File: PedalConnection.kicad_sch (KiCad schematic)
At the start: 17 parts, among them U1 OPA325IDBVR, U10 OPA325IDBVR, U3 VOM618A-3T

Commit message: made connector match drawing
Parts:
- renumbered C6 to C3, C3 to C4, R8 to R15, R11 to R16, R22 to R17, R1 to R18, R23 to R19, R2 to R20, R24 to R21, R3 to R22, R25 to R23, R4 to R24, R26 to R25, R5 to R26, U3 to U7, U10 to U8, U1 to U9
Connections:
- net GNDp is gone; now on net GND: U7.2

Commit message: placed most components
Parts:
- R18: renamed from R15; footprint (none) -> Resistor_SMD:R_0805_2012Metric
- R19: renamed from R16; footprint (none) -> Resistor_SMD:R_0805_2012Metric
- R20: renamed from R17; footprint (none) -> Resistor_SMD:R_0805_2012Metric
- R21: renamed from R18; footprint (none) -> Resistor_SMD:R_0805_2012Metric
- R22: renamed from R19; footprint (none) -> Resistor_SMD:R_0805_2012Metric
- R23: renamed from R20; footprint (none) -> Resistor_SMD:R_0805_2012Metric
- R24: renamed from R21; footprint (none) -> Resistor_SMD:R_0805_2012Metric
- R25: renamed from R22; footprint (none) -> Resistor_SMD:R_0805_2012Metric
- R26: renamed from R23; footprint (none) -> Resistor_SMD:R_0805_2012Metric
- R27: renamed from R24; footprint (none) -> Resistor_SMD:R_0805_2012Metric
- R28: renamed from R25; footprint (none) -> Resistor_SMD:R_0805_2012Metric
- R29: renamed from R26; footprint (none) -> Resistor_SMD:R_0805_2012Metric
- renumbered C3 to C6, C4 to C7, U8 to U10, U9 to U11, U7 to U9

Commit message: Finalized analog components. Everything is done 🙏
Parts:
- removed R28, R29: R_US, Resistor_SMD:R_0805_2012Metric, symbol Device:R_US
- added R6: 100R, Resistor_SMD:R_0805_2012Metric, symbol Device:R_US
- added R7: 10k, Resistor_SMD:R_0805_2012Metric, symbol Device:R_US
- C6, C7: footprint (none) -> Capacitor_SMD:C_0805_2012Metric
- R20: value R_US -> 100R
- R21, R22, R23, R24, R26: value R_US -> 10k
- R25, R27: value R_US -> 1k
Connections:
- net BrakeIO: now also R27.2
- net GND: now also R21.1, R23.1, R6.2; no longer R21.2, R25.1, R27.1
- net Throttle+: now also R6.1, R7.1; no longer R21.1, R23.1
- net ThrottleIO: now also R25.2
- net at U11.1 (OUT): now also R23.2, R25.1; no longer R27.2
- net at R26.2, U10.1 (OUT): now also R27.1
- new net: R21.2, R7.2, U11.3 (+IN)

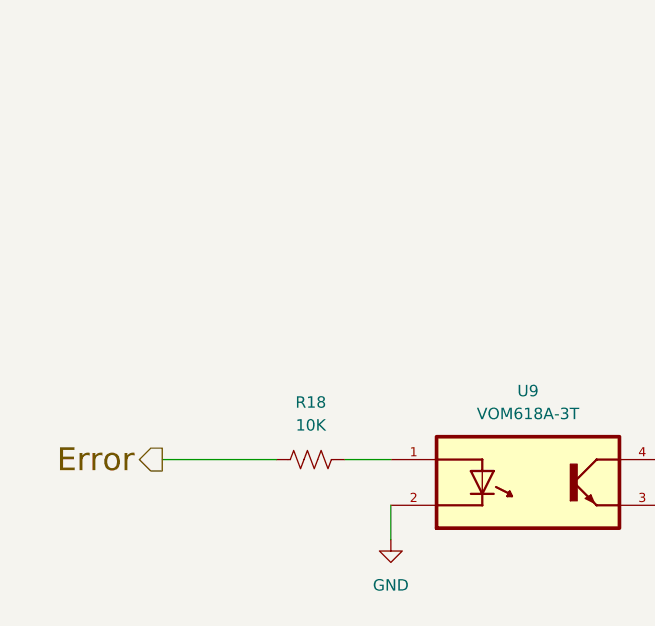
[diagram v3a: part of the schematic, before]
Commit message: added LED indicators, fixed footprints
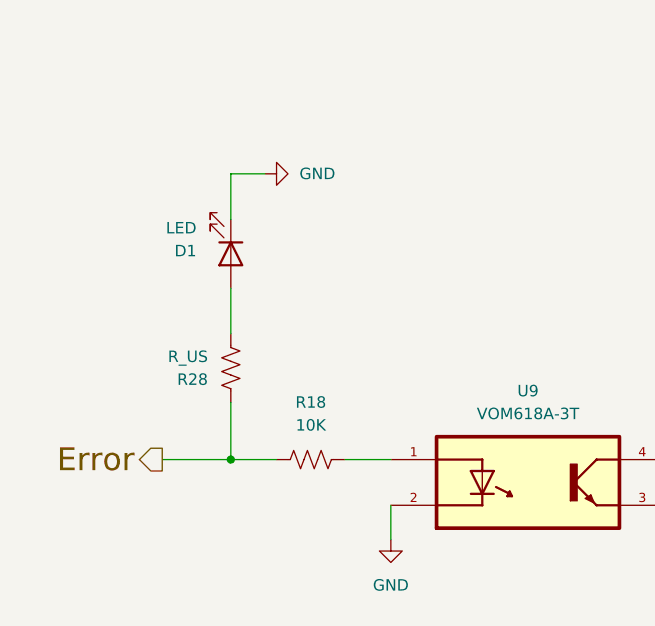
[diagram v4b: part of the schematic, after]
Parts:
- added D1: LED, LED_SMD:LED_0805_2012Metric, symbol Device:LED
- added R28: R_US, Resistor_SMD:R_0805_2012Metric, symbol Device:R_US
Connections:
- net Error: now also R28.1
- net GND: now also D1.1 (K)
- new net: D1.2 (A), R28.2

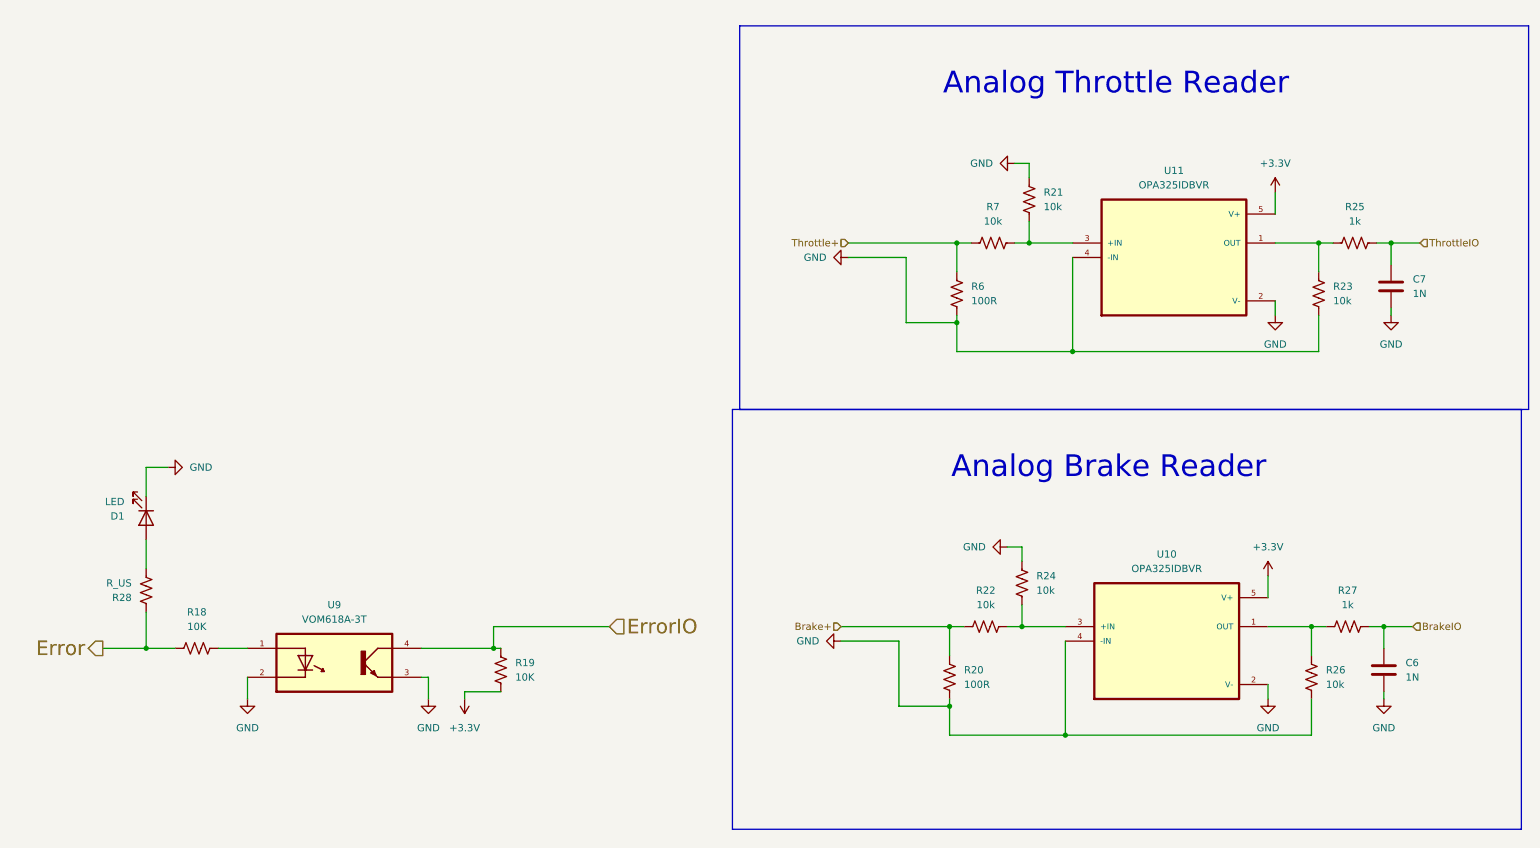
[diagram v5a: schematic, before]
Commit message: redid 35 pos pinout
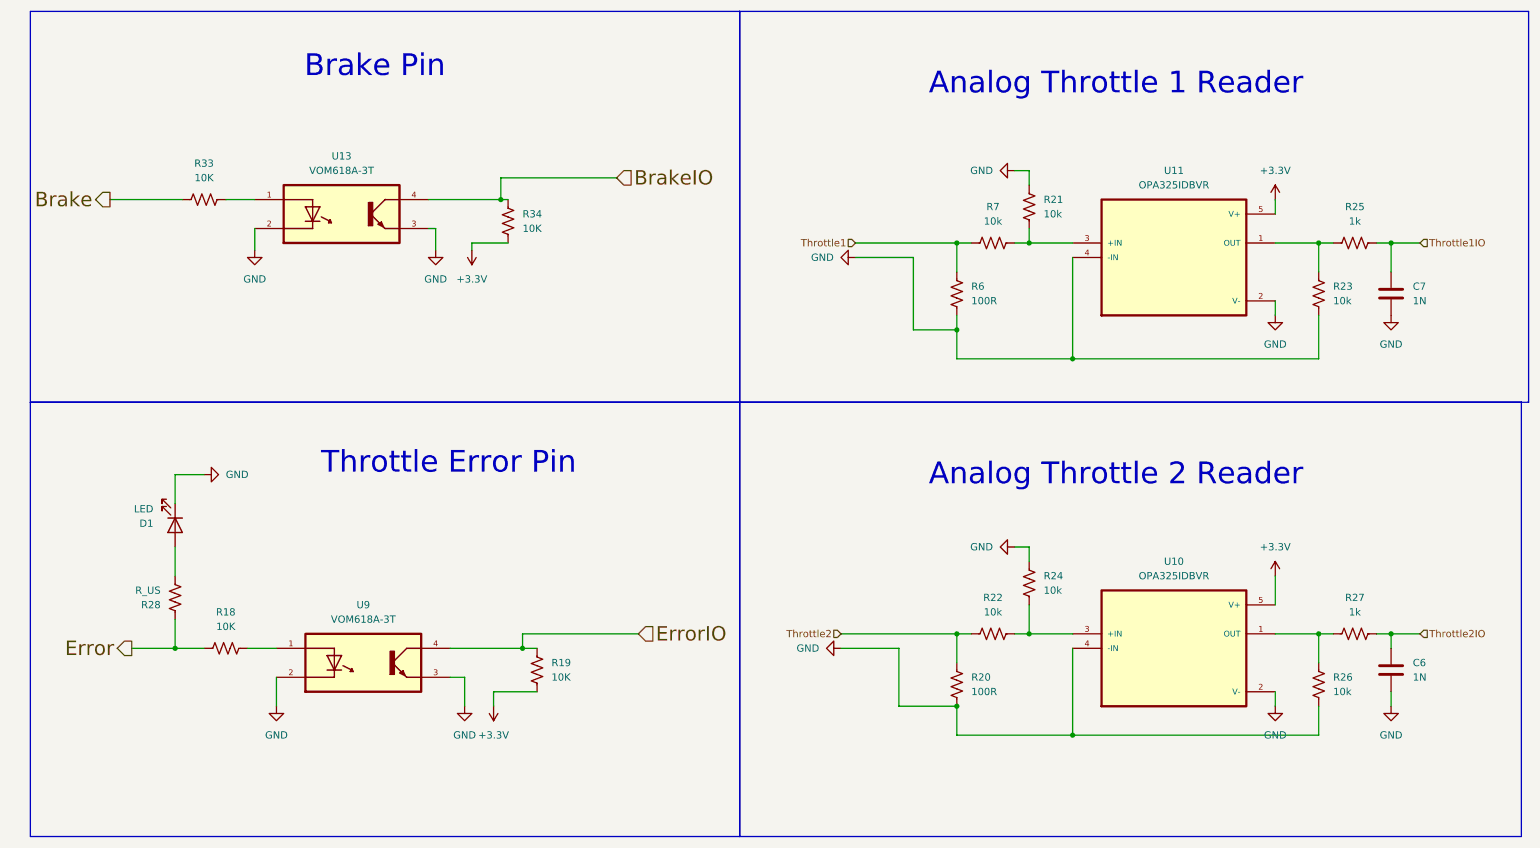
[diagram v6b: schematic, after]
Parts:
- added R33, R34: 10K, Resistor_SMD:R_0805_2012Metric, symbol Device:R_US
- added U13: VOM618A-3T, VOM618A-3T:SOIC254P695X242-4N, symbol VOM618A-3T:VOM618A-3T
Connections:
- net +3.3V: now also R34.2
- net BrakeIO: now also R34.1, U13.4; no longer C6.1, R27.2
- net GND: now also U13.2, U13.3
- net Brake+ renamed Throttle2
- net Throttle+ renamed Throttle1
- net ThrottleIO renamed Throttle1IO
- new net: R33.2, U13.1
- new net Brake: R33.1
- new net Throttle2IO: C6.1, R27.2
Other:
- note added: "Analog Throttle 1 Reader"
- note added: "Analog Throttle 2 Reader"
- note added: "Brake Pin"
- note added: "Throttle Error Pin"
- note removed: "Analog Brake Reader"
- note removed: "Analog Throttle Reader"
- moved on the sheet: C6, C7, D1, R18, R19, R20, R21, R22, R24, R26, R27, R28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

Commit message: complete. Minor Tweaks
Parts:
- removed D1: LED, LED_SMD:LED_0805_2012Metric, symbol Device:LED
- removed R28: R_US, Resistor_SMD:R_0805_2012Metric, symbol Device:R_US

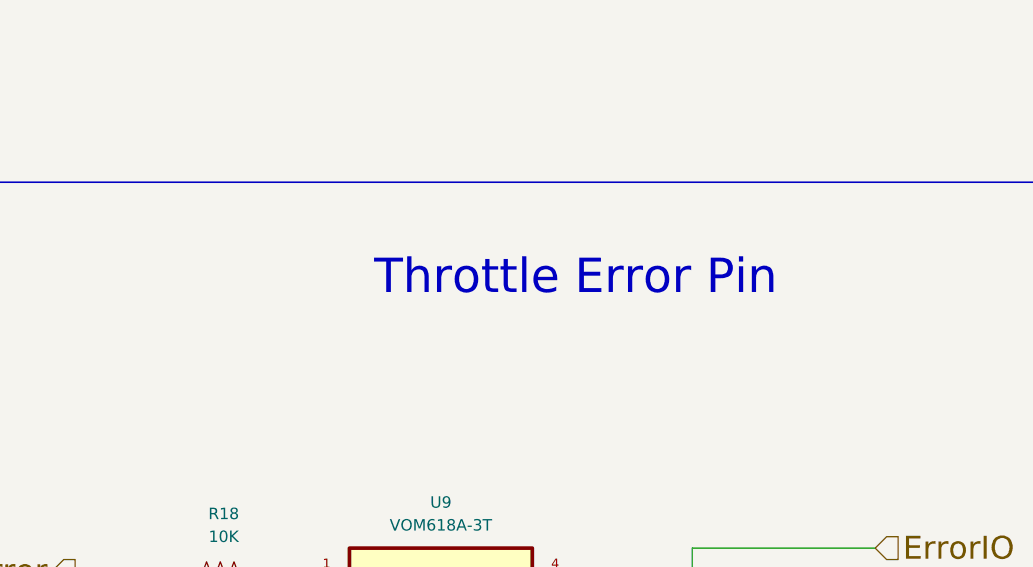
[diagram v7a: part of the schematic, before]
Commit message: fixed mounting holes
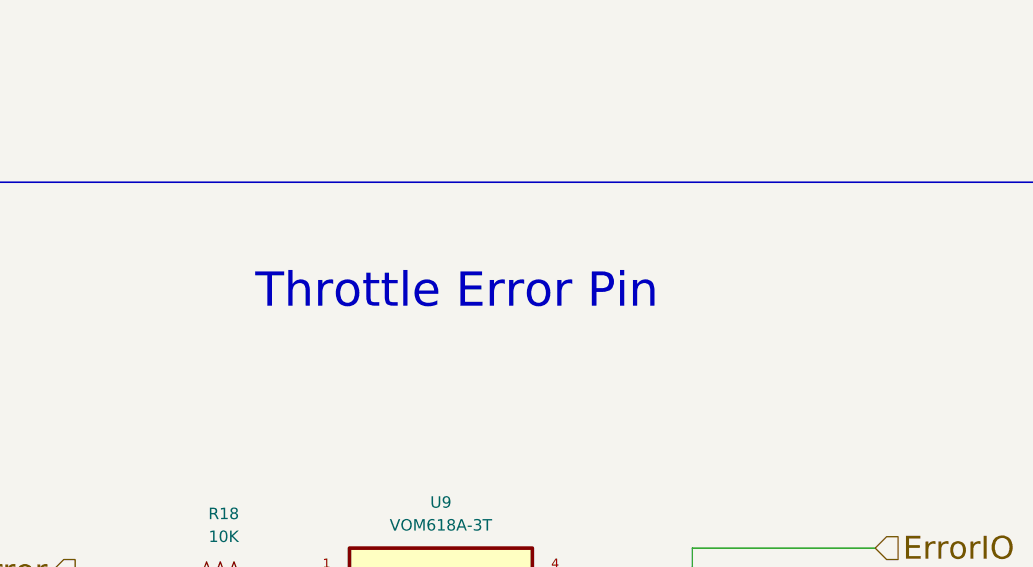
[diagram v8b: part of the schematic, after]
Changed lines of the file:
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@@
 	(text "Throttle Error Pin"
 		(exclude_from_sim no)
-		(at 91.186 94.488 0)
+		(at 77.978 96.012 0)
 		(effects
 			(font
